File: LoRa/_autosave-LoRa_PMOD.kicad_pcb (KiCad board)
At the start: 2 copper layers, 38.1 x 20 mm, 7 parts, among them P1 PMOD_LoRa, P2 Ext, U1 RFM95W-868S2

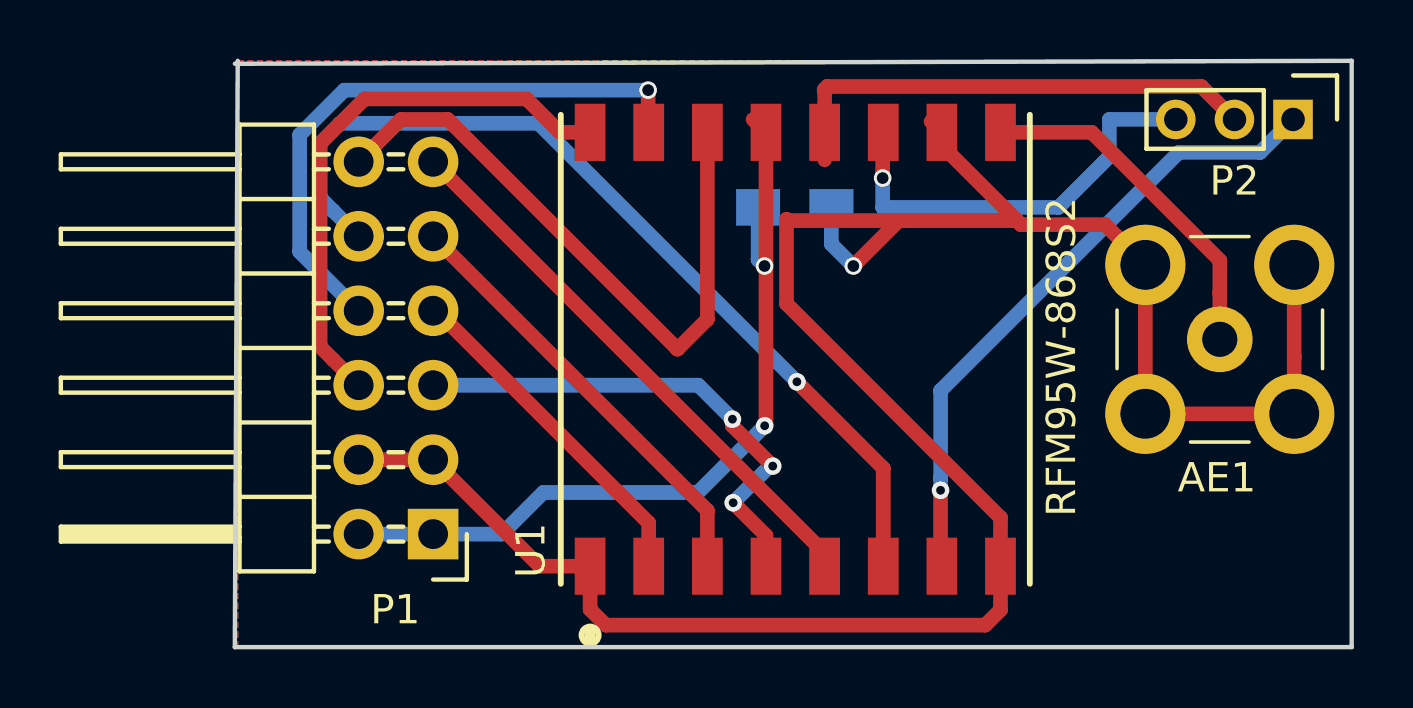
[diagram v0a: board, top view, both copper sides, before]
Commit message: Adding new render pictures
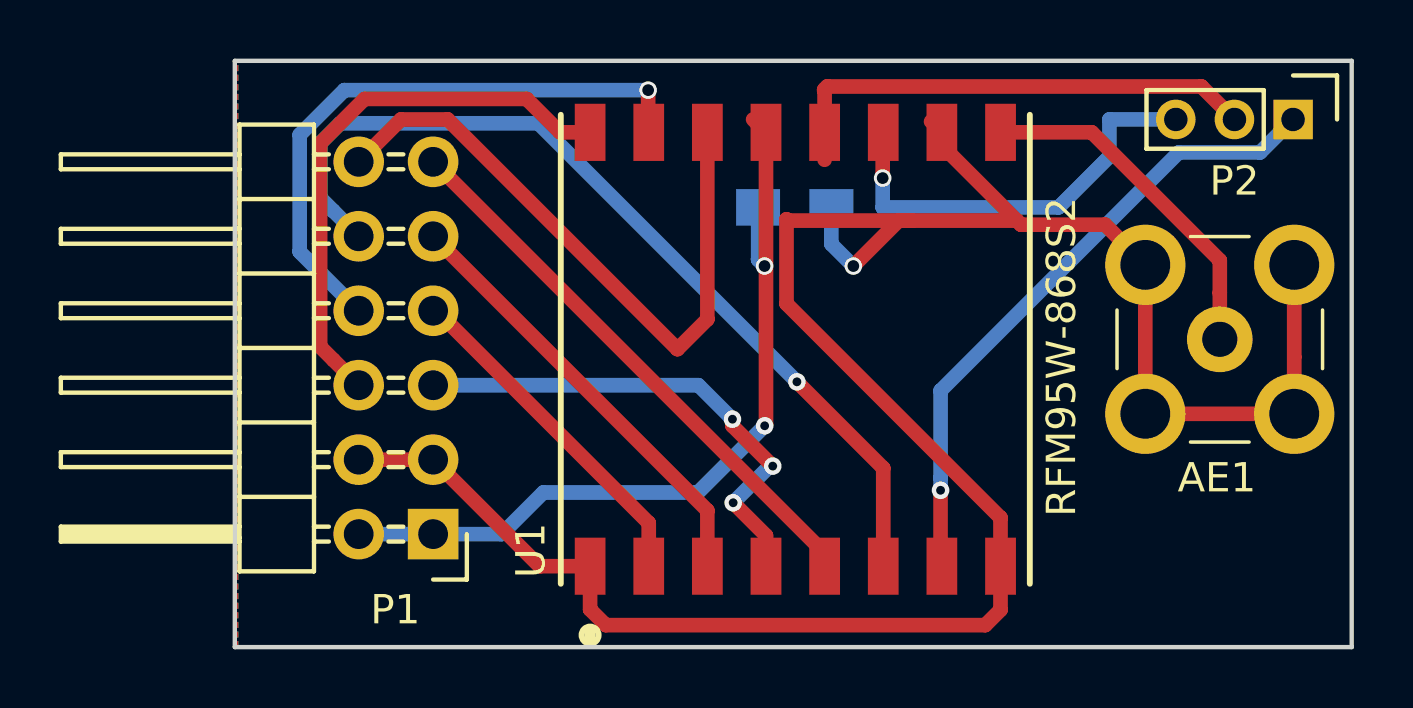
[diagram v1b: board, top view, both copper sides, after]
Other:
- outline, holes or cut-outs redrawn
- board text added: "LoRa-PMOD"
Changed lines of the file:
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@@
   (general
     (thickness 1.6)
-    (drawings 16)
+    (drawings 17)
     (tracks 146)
     (zones 0)
@@
   (page A4)
   (layers
-    (0 F.Cu signal)
+    (0 F.Cu signal hide)
     (31 B.Cu signal)
     (32 B.Adhes user hide)
@@
     (37 F.SilkS user)
     (38 B.Mask user)
-    (39 F.Mask user)
+    (39 F.Mask user hide)
     (40 Dwgs.User user hide)
     (41 Cmts.User user hide)
@@
     (pad 12 thru_hole oval (at 2.54 12.7 180) (size 1.7272 1.7272) (drill 1.016) (layers *.Cu *.Mask)
       (net 7 DIO0))
-    (model Pin_Headers.3dshapes/Pin_Header_Angled_2x06.wrl
-      (offset (xyz 1.269999980926514 -6.349999904632568 0))
-      (scale (xyz 1 1 1))
-      (rotate (xyz 0 0 90))
-    )
-    (model ${KISYS3DMOD}/Connector_PinHeader_1.00mm.3dshapes/PinHeader_2x08_P1.00mm_Horizontal.wrl
-      (at (xyz 0 0 0))
-      (scale (xyz 1.8 1.8 1))
-      (rotate (xyz 0 0 0))
-    )
   )
   (module Pin_Headers:Pin_Header_Straight_1x03_Pitch2.00mm (layer F.Cu)
@@
       (xy -2.859194 -0.90424) (xy -2.847818 -0.905006)) (layer B.SilkS) (width 0.01))
   )
+  (gr_text LoRa-PMOD (at 99.8 102) (layer B.SilkS)
+    (effects (font (size 1 1) (thickness 0.2)) (justify mirror))
+  )
   (gr_line (start 132 101) (end 132 121) (layer Edge.Cuts) (width 0.15))
-  (gr_line (start 93.9 101.1) (end 132 101) (layer Edge.Cuts) (width 0.15))
-  (gr_line (start 93.9 121) (end 94 101) (layer Edge.Cuts) (width 0.15))
+  (gr_line (start 93.9 101) (end 132 101) (layer Edge.Cuts) (width 0.15))
+  (gr_line (start 93.9 121) (end 93.9 101) (layer Edge.Cuts) (width 0.15))
   (gr_line (start 132 121) (end 93.9 121) (layer Edge.Cuts) (width 0.15))
   (gr_text IO0 (at 95.8 104.7) (layer B.SilkS)
